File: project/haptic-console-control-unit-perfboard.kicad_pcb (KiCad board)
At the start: 2 copper layers, 90 x 144 mm, 36 parts, among them J1 JST-XH-5, J2 JST-XH-5

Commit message: Eliminate collinear wire overlaps in perfboard jumper wiring
The back-side jumper wires are decorative footprints (no pads, no nets,
invisible to DRC), so their only quality bar is legibility -- and 55 pairs
were merging into each other. The prior session's z-tier stagger fixed
mid-span crossings but not collinear overlaps: two wires sharing a row or
column with overlapping spans, which no height offset can hide.

Rewrote the generator around a span registry -- (net, lo, hi, tier) per grid
line, checked at emit time, rejecting any leg that would overlap another net
at the same tier. That makes "no overlaps" true by construction rather than
by inspection. Tiers now come from greedy-colouring the net-conflict graph
instead of bumping individual segments, which could silently recreate an
overlap at the tier it moved to. 268 segments, 0 same-tier overlaps (was 163
segments, 55 overlaps).

Four real bugs surfaced while getting there:

- taps.json was corrupt ground truth: derived from the old wire geometry, it
  recorded elbow corner points as taps, several of which sit on unrelated
  components' pads -- routing to those invents connections that don't exist.
  Rebuilt from wire labels' REF.PIN->REF.PIN text against real pad positions.

- Routing only on pad-free lanes cannot work here: 4 of ~36 columns and 14 of
  ~54 rows are pad-free and all hug the edges, leaving 19 of 37 signal nets
  unroutable. Legs may follow pad lines as long as they don't pass through a pad.

- Not every pad is on the 2.54mm grid (JST rows at y=15.44 vs 15.24). Grid-only
  routing forced a sub-millimetre hop off each such pad, which the stub filter
  then deleted, silently disconnecting nets from their own pins.

- Wires centred on the edge column overhung the board by their tube radius
  despite being in bounds by centreline.

Added verify_v3.py as a standing check: every tap must lie on a wire and each
net's segments must form one connected component. It caught the open-circuit
bug above, whic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
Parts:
- added W1: GND CB3.2->CB4.2, , B.Cu at (17.8, 49.5)
- added W10: GND CB3.2->CB4.2, , B.Cu at (43.2, 111.9)
- added W100: D27 B8.2->J_TEENSY_B.19, , B.Cu at (48.3, 49.5)
- added W101: D27 B8.2->J_TEENSY_B.19, , B.Cu at (47.0, 58.4)
- added W102: D27 B8.2->J_TEENSY_B.19, , B.Cu at (52.1, 61.2)
- added W103: D27 B8.2->J_TEENSY_B.19, , B.Cu at (58.4, 67.4)
- added W104: D24 B5.2->J_TEENSY_B.16, , B.Cu at (77.5, 38.1)
- added W105: D24 B5.2->J_TEENSY_B.16, , B.Cu at (78.7, 48.4)
- added W106: D24 B5.2->J_TEENSY_B.16, , B.Cu at (66.0, 58.7)
- added W107: D24 B5.2->J_TEENSY_B.16, , B.Cu at (53.3, 66.2)
- added W108: D24 B5.2->J_TEENSY_B.16, , B.Cu at (52.1, 73.7)
- added W109: D25 B6.2->J_TEENSY_B.17, , B.Cu at (66.0, 39.4)
- added W11: GND CB3.2->CB4.2, , B.Cu at (7.62, 34.3)
- added W110: D25 B6.2->J_TEENSY_B.17, , B.Cu at (62.2, 40.6)
- added W111: D25 B6.2->J_TEENSY_B.17, , B.Cu at (58.4, 49.5)
- added W112: D25 B6.2->J_TEENSY_B.17, , B.Cu at (57.1, 58.4)
- added W113: D25 B6.2->J_TEENSY_B.17, , B.Cu at (55.9, 66.0)
- added W114: D25 B6.2->J_TEENSY_B.17, , B.Cu at (54.6, 73.7)
- added W115: D26 B7.2->J_TEENSY_B.18, , B.Cu at (55.9, 36.9)
- added W116: D26 B7.2->J_TEENSY_B.18, , B.Cu at (55.9, 75.0)
- added W117: D26 B7.2->J_TEENSY_B.18, , B.Cu at (62.2, 35.6)
- added W118: D26 B7.2->J_TEENSY_B.18, , B.Cu at (68.6, 38.1)
- added W119: D26 B7.2->J_TEENSY_B.18, , B.Cu at (72.4, 40.6)
- added W12: GND CB3.2->CB4.2, , B.Cu at (45.7, 34.3)
- added W120: D26 B7.2->J_TEENSY_B.18, , B.Cu at (76.2, 58.4)
- added W121: D26 B7.2->J_TEENSY_B.18, , B.Cu at (66.0, 76.2)
- added W122: D14 CB5.1->J_TEENSY_A.13, , B.Cu at (69.8, 119.4)
- added W123: D14 CB5.1->J_TEENSY_A.13, , B.Cu at (71.1, 104.1)
- added W124: D14 CB5.1->J_TEENSY_A.13, , B.Cu at (61.0, 88.9)
- added W125: D14 CB5.1->J_TEENSY_A.13, , B.Cu at (50.8, 55.9)
- added W126: D14 CB5.1->J_TEENSY_A.13, , B.Cu at (50.8, 81.3)
- added W127: D14 CB5.1->J_TEENSY_A.13, , B.Cu at (49.5, 73.7)
- added W128: D14 CB5.1->J_TEENSY_A.13, , B.Cu at (48.3, 66.1)
- added W129: D14 CB5.1->J_TEENSY_A.13, , B.Cu at (49.5, 58.4)
- added W13: GND CB3.2->CB4.2, , B.Cu at (17.8, 73.7)
- added W130: D14 CB5.1->J_TEENSY_A.13, , B.Cu at (47.0, 53.3)
- added W131: D14 CB5.1->J_TEENSY_A.13, , B.Cu at (43.2, 55.9)
- added W132: D13 CB4.1->J_TEENSY_A.14, , B.Cu at (55.9, 118.1)
- added W133: D13 CB4.1->J_TEENSY_A.14, , B.Cu at (47.0, 116.8)
- added W134: D13 CB4.1->J_TEENSY_A.14, , B.Cu at (38.1, 54.6)
- added W135: D13 CB4.1->J_TEENSY_A.14, , B.Cu at (38.1, 95.3)
- added W136: D13 CB4.1->J_TEENSY_A.14, , B.Cu at (36.8, 73.7)
- added W137: D13 CB4.1->J_TEENSY_A.14, , B.Cu at (35.6, 66.1)
- added W138: D13 CB4.1->J_TEENSY_A.14, , B.Cu at (36.8, 58.4)
- added W139: D13 CB4.1->J_TEENSY_A.14, , B.Cu at (41.9, 50.8)
- added W14: GND CB3.2->CB4.2, , B.Cu at (15.2, 66.0)
- added W140: D13 CB4.1->J_TEENSY_A.14, , B.Cu at (45.7, 54.6)
- added W141: D36 R3.2->J_TEENSY_A.21, , B.Cu at (54.6, 124.5)
- added W142: D36 R3.2->J_TEENSY_A.21, , B.Cu at (55.9, 121.9)
- added W143: D36 R3.2->J_TEENSY_A.21, , B.Cu at (61.0, 119.4)
- added W144: D36 R3.2->J_TEENSY_A.21, , B.Cu at (66.0, 96.5)
- added W145: D36 R3.2->J_TEENSY_A.21, , B.Cu at (64.8, 73.7)
- added W146: D36 R3.2->J_TEENSY_A.21, , B.Cu at (63.5, 66.1)
- added W147: D38 R5.2->J_TEENSY_A.19, , B.Cu at (80.0, 124.5)
- added W148: D38 R5.2->J_TEENSY_A.19, , B.Cu at (81.3, 97.8)
- added W149: D38 R5.2->J_TEENSY_A.19, , B.Cu at (71.1, 71.1)
- added W15: GND CB3.2->CB4.2, , B.Cu at (16.5, 58.4)
- added W150: D38 R5.2->J_TEENSY_A.19, , B.Cu at (61.0, 64.8)
- added W151: D38 R5.2->J_TEENSY_A.19, , B.Cu at (59.7, 58.4)
- added W152: D37 R4.2->J_TEENSY_A.20, , B.Cu at (66.0, 55.9)
- added W153: D37 R4.2->J_TEENSY_A.20, , B.Cu at (66.0, 121.9)
- added W154: D37 R4.2->J_TEENSY_A.20, , B.Cu at (67.3, 119.4)
- added W155: D37 R4.2->J_TEENSY_A.20, , B.Cu at (68.6, 66.1)
- added W156: D37 R4.2->J_TEENSY_A.20, , B.Cu at (68.6, 121.9)
- added W157: D37 R4.2->J_TEENSY_A.20, , B.Cu at (72.4, 124.5)
- added W158: D37 R4.2->J_TEENSY_A.20, , B.Cu at (76.2, 106.7)
- added W159: D37 R4.2->J_TEENSY_A.20, , B.Cu at (73.7, 88.9)
- added W16: GND CB3.2->CB4.2, , B.Cu at (48.3, 49.5)
- added W160: D37 R4.2->J_TEENSY_A.20, , B.Cu at (71.1, 81.3)
- added W161: D37 R4.2->J_TEENSY_A.20, , B.Cu at (69.8, 73.7)
- added W162: D37 R4.2->J_TEENSY_A.20, , B.Cu at (67.3, 58.4)
- added W163: D37 R4.2->J_TEENSY_A.20, , B.Cu at (63.5, 53.3)
- added W164: D37 R4.2->J_TEENSY_A.20, , B.Cu at (61.0, 55.9)
- added W165: D35 NP1.8->J_TEENSY_A.22, , B.Cu at (78.7, 60.0)
- added W166: D35 NP1.8->J_TEENSY_A.22, , B.Cu at (72.4, 61.2)
- added W167: D35 NP1.8->J_TEENSY_A.22, , B.Cu at (66.0, 59.8)
- added W168: D34 NP1.7->J_TEENSY_A.23, , B.Cu at (78.7, 62.4)
- added W169: D34 NP1.7->J_TEENSY_A.23, , B.Cu at (74.9, 63.5)
- added W17: GND CB3.2->CB4.2, , B.Cu at (22.9, 81.4)
- added W170: D34 NP1.7->J_TEENSY_A.23, , B.Cu at (71.1, 61.0)
- added W171: D34 NP1.7->J_TEENSY_A.23, , B.Cu at (69.8, 58.4)
- added W172: D33 NP1.6->J_TEENSY_A.24, , B.Cu at (55.9, 63.7)
- added W173: D33 NP1.6->J_TEENSY_A.24, , B.Cu at (33.0, 61.1)
- added W174: D33 NP1.6->J_TEENSY_A.24, , B.Cu at (31.8, 58.4)
- added W175: D33 NP1.6->J_TEENSY_A.24, , B.Cu at (30.5, 53.3)
- added W176: D33 NP1.6->J_TEENSY_A.24, , B.Cu at (50.8, 48.3)
- added W177: D33 NP1.6->J_TEENSY_A.24, , B.Cu at (71.1, 53.3)
- added W178: D32 NP1.5->J_TEENSY_B.24, , B.Cu at (74.9, 66.2)
- added W179: D32 NP1.5->J_TEENSY_B.24, , B.Cu at (71.1, 69.9)
- added W18: GND CB3.2->CB4.2, , B.Cu at (20.3, 100.5)
- added W180: D31 NP1.4->J_TEENSY_B.23, , B.Cu at (72.4, 68.7)
- added W181: D31 NP1.4->J_TEENSY_B.23, , B.Cu at (66.0, 71.2)
- added W182: D31 NP1.4->J_TEENSY_B.23, , B.Cu at (67.3, 73.7)
- added W183: D30 NP1.3->J_TEENSY_B.22, , B.Cu at (73.7, 71.2)
- added W184: D30 NP1.3->J_TEENSY_B.22, , B.Cu at (68.6, 72.4)
- added W185: D30 NP1.3->J_TEENSY_B.22, , B.Cu at (67.3, 73.7)
- added W186: D0 J1.1->J_TEENSY_B.2, , B.Cu at (19.1, 99.1)
- added W187: D0 J1.1->J_TEENSY_B.2, , B.Cu at (15.2, 86.4)
- added W188: D10 CB1.1->J_TEENSY_B.12, , B.Cu at (24.1, 119.4)
- added W189: D10 CB1.1->J_TEENSY_B.12, , B.Cu at (30.5, 118.1)
- added W19: GND CB3.2->CB4.2, , B.Cu at (21.6, 89.1)
- added W190: D10 CB1.1->J_TEENSY_B.12, , B.Cu at (35.6, 116.9)
- added W191: D10 CB1.1->J_TEENSY_B.12, , B.Cu at (40.6, 95.3)
- added W192: D1 J1.2->J_TEENSY_B.3, , B.Cu at (21.6, 96.6)
- added W193: D1 J1.2->J_TEENSY_B.3, , B.Cu at (20.3, 85.1)
- added W194: D1 J1.2->J_TEENSY_B.3, , B.Cu at (19.1, 73.7)
- added W195: D2 J1.3->J_TEENSY_B.4, , B.Cu at (24.1, 94.1)
- added W196: D2 J1.3->J_TEENSY_B.4, , B.Cu at (25.4, 91.6)
- added W197: D2 J1.3->J_TEENSY_B.4, , B.Cu at (24.1, 89.1)
- added W198: D2 J1.3->J_TEENSY_B.4, , B.Cu at (22.9, 81.4)
- added W199: D2 J1.3->J_TEENSY_B.4, , B.Cu at (21.6, 73.7)
- added W2: GND CB3.2->CB4.2, , B.Cu at (17.8, 114.4)
- added W20: GND CB3.2->CB4.2, , B.Cu at (59.7, 89.1)
- added W200: D3 J1.4->J_TEENSY_B.5, , B.Cu at (25.4, 91.6)
- added W201: D3 J1.4->J_TEENSY_B.5, , B.Cu at (27.9, 90.3)
- added W202: D3 J1.4->J_TEENSY_B.5, , B.Cu at (26.7, 89.1)
- added W203: D3 J1.4->J_TEENSY_B.5, , B.Cu at (25.4, 81.4)
- added W204: D3 J1.4->J_TEENSY_B.5, , B.Cu at (24.1, 73.7)
- added W205: D4 J2.1->J_TEENSY_B.6, , B.Cu at (59.7, 99.1)
- added W206: D4 J2.1->J_TEENSY_B.6, , B.Cu at (58.4, 94.1)
- added W207: D4 J2.1->J_TEENSY_B.6, , B.Cu at (43.2, 89.1)
- added W208: D4 J2.1->J_TEENSY_B.6, , B.Cu at (27.9, 81.4)
- added W209: D4 J2.1->J_TEENSY_B.6, , B.Cu at (26.7, 73.7)
- added W21: GND CB3.2->CB4.2, , B.Cu at (58.4, 100.5)
- added W210: D5 J2.2->J_TEENSY_B.7, , B.Cu at (45.7, 96.6)
- added W211: D5 J2.2->J_TEENSY_B.7, , B.Cu at (30.5, 85.1)
- added W212: D5 J2.2->J_TEENSY_B.7, , B.Cu at (29.2, 73.7)
- added W213: D8 R1.2->J_TEENSY_B.10, , B.Cu at (27.9, 110.5)
- added W214: D8 R1.2->J_TEENSY_B.10, , B.Cu at (31.8, 96.5)
- added W215: D8 R1.2->J_TEENSY_B.10, , B.Cu at (35.6, 85.1)
- added W216: D6 J2.3->J_TEENSY_B.8, , B.Cu at (53.3, 94.1)
- added W217: D6 J2.3->J_TEENSY_B.8, , B.Cu at (45.7, 83.9)
- added W218: D6 J2.3->J_TEENSY_B.8, , B.Cu at (44.5, 73.7)
- added W219: D6 J2.3->J_TEENSY_B.8, , B.Cu at (43.2, 72.4)
- added W22: +3V3 S6.2->R12.2, , B.Cu at (44.5, 25.4)
- added W220: D6 J2.3->J_TEENSY_B.8, , B.Cu at (36.8, 71.2)
- added W221: D6 J2.3->J_TEENSY_B.8, , B.Cu at (30.5, 72.4)
- added W222: D11 CB2.1->J_TEENSY_B.13, , B.Cu at (36.8, 119.4)
- added W223: D11 CB2.1->J_TEENSY_B.13, , B.Cu at (43.2, 92.8)
- added W224: D11 CB2.1->J_TEENSY_B.13, , B.Cu at (43.2, 118.1)
- added W225: D11 CB2.1->J_TEENSY_B.13, , B.Cu at (44.5, 116.9)
- added W226: D11 CB2.1->J_TEENSY_B.13, , B.Cu at (45.7, 114.4)
- added W227: D11 CB2.1->J_TEENSY_B.13, , B.Cu at (44.5, 111.9)
- added W228: D7 J2.4->J_TEENSY_B.9, , B.Cu at (54.6, 91.6)
- added W229: D7 J2.4->J_TEENSY_B.9, , B.Cu at (48.3, 82.6)
- added W23: +3V3 S6.2->R12.2, , B.Cu at (50.8, 29.2)
- added W230: D7 J2.4->J_TEENSY_B.9, , B.Cu at (47.0, 73.7)
- added W231: D7 J2.4->J_TEENSY_B.9, , B.Cu at (45.7, 72.4)
- added W232: D7 J2.4->J_TEENSY_B.9, , B.Cu at (39.4, 71.1)
- added W233: D7 J2.4->J_TEENSY_B.9, , B.Cu at (33.0, 72.4)
- added W234: D9 R2.2->J_TEENSY_B.11, , B.Cu at (36.8, 124.5)
- added W235: D9 R2.2->J_TEENSY_B.11, , B.Cu at (33.0, 120.7)
- added W236: D9 R2.2->J_TEENSY_B.11, , B.Cu at (21.6, 116.8)
- added W237: D9 R2.2->J_TEENSY_B.11, , B.Cu at (10.2, 92.8)
- added W238: D9 R2.2->J_TEENSY_B.11, , B.Cu at (24.1, 68.7)
- added W239: D9 R2.2->J_TEENSY_B.11, , B.Cu at (38.1, 71.2)
- added W24: +3V3 S6.2->R12.2, , B.Cu at (63.5, 29.2)
- added W240: D12 CB3.1->J_TEENSY_B.14, , B.Cu at (43.2, 118.1)
- added W241: D12 CB3.1->J_TEENSY_B.14, , B.Cu at (44.5, 116.9)
- added W242: D12 CB3.1->J_TEENSY_B.14, , B.Cu at (45.7, 95.3)
- added W243: D28 NP1.1->J_TEENSY_B.20, , B.Cu at (78.7, 82.6)
- added W244: D28 NP1.1->J_TEENSY_B.20, , B.Cu at (69.8, 89.1)
- added W245: D28 NP1.1->J_TEENSY_B.20, , B.Cu at (61.0, 81.4)
- added W246: D29 NP1.2->J_TEENSY_B.21, , B.Cu at (78.7, 72.5)
- added W247: D29 NP1.2->J_TEENSY_B.21, , B.Cu at (69.8, 71.2)
- added W248: D29 NP1.2->J_TEENSY_B.21, , B.Cu at (61.0, 72.4)
- added W249: D29 NP1.2->J_TEENSY_B.21, , B.Cu at (62.2, 73.7)
- added W25: +3V3 S6.2->R12.2, , B.Cu at (20.3, 58.4)
- added W250: LED_ARM CB1.3->R1.1, , B.Cu at (17.8, 115.6)
- added W251: LED_ARM CB1.3->R1.1, , B.Cu at (16.5, 116.9)
- added W252: LED_ARM CB1.3->R1.1, , B.Cu at (15.2, 120.7)
- added W253: LED_ARM CB1.3->R1.1, , B.Cu at (16.5, 124.5)
- added W254: LED_EN CB2.3->R2.1, , B.Cu at (30.5, 115.6)
- added W255: LED_EN CB2.3->R2.1, , B.Cu at (30.5, 121.9)
- added W256: LED_EN CB2.3->R2.1, , B.Cu at (29.2, 116.8)
- added W257: LED_EN CB2.3->R2.1, , B.Cu at (27.9, 118.1)
- added W258: LED_EN CB2.3->R2.1, , B.Cu at (29.2, 119.4)
- added W259: LED_SFT CB3.3->R3.1, , B.Cu at (43.2, 115.6)
- added W26: +3V3 S6.2->R12.2, , B.Cu at (22.9, 41.9)
- added W260: LED_SFT CB3.3->R3.1, , B.Cu at (41.9, 116.9)
- added W261: LED_SFT CB3.3->R3.1, , B.Cu at (40.6, 120.7)
- added W262: LED_SFT CB3.3->R3.1, , B.Cu at (41.9, 124.5)
- added W263: LED_CONF CB4.3->R4.1, , B.Cu at (57.1, 114.4)
- added W264: LED_CONF CB4.3->R4.1, , B.Cu at (58.4, 119.4)
- added W265: LED_CONF CB4.3->R4.1, , B.Cu at (57.1, 124.5)
- added W266: LED_ALT CB5.3->R5.1, , B.Cu at (67.3, 114.4)
- added W267: LED_ALT CB5.3->R5.1, , B.Cu at (66.0, 119.4)
- added W268: LED_ALT CB5.3->R5.1, , B.Cu at (67.3, 124.5)
- added W27: +3V3 S6.2->R12.2, , B.Cu at (64.8, 73.7)
- added W28: +3V3 S6.2->R12.2, , B.Cu at (81.3, 53.3)
- added W29: +3V3 S6.2->R12.2, , B.Cu at (66.0, 33.0)
- added W3: GND CB3.2->CB4.2, , B.Cu at (30.5, 114.4)
- added W30: +5V S6.3->J_TEENSY_A.1, , B.Cu at (44.5, 22.9)
- added W31: +5V S6.3->J_TEENSY_A.1, , B.Cu at (81.3, 22.9)
- added W32: +5V S6.3->J_TEENSY_A.1, , B.Cu at (12.7, 40.7)
- added W33: SCL R13.1->J_TEENSY_A.8, , B.Cu at (44.5, 17.9)
- added W34: SCL R13.1->J_TEENSY_A.8, , B.Cu at (81.3, 17.9)
- added W35: SCL R13.1->J_TEENSY_A.8, , B.Cu at (53.3, 25.5)
- added W36: SCL R13.1->J_TEENSY_A.8, , B.Cu at (33.0, 58.4)
- added W37: SCL R13.1->J_TEENSY_A.8, , B.Cu at (35.6, 38.2)
- added W38: SDA S6.4->R12.1, , B.Cu at (44.5, 20.4)
- added W39: SDA S6.4->R12.1, , B.Cu at (81.3, 20.4)
- added W4: GND CB3.2->CB4.2, , B.Cu at (43.2, 114.4)
- added W40: SDA S6.4->R12.1, , B.Cu at (38.1, 33.0)
- added W41: SDA S6.4->R12.1, , B.Cu at (43.2, 26.7)
- added W42: SDA S6.4->R12.1, , B.Cu at (33.0, 45.7)
- added W43: IRQ1 S1.6->J_TEENSY_A.12, , B.Cu at (6.35, 15.4)
- added W44: IRQ1 S1.6->J_TEENSY_A.12, , B.Cu at (5.08, 37.1)
- added W45: IRQ1 S1.6->J_TEENSY_A.12, , B.Cu at (22.9, 58.7)
- added W46: IRQ1 S1.6->J_TEENSY_A.12, , B.Cu at (40.6, 58.6)
- added W47: IRQ2 S2.6->J_TEENSY_A.11, , B.Cu at (20.3, 15.3)
- added W48: IRQ2 S2.6->J_TEENSY_A.11, , B.Cu at (11.4, 15.2)
- added W49: IRQ2 S2.6->J_TEENSY_A.11, , B.Cu at (2.54, 38.1)
- added W5: GND CB3.2->CB4.2, , B.Cu at (55.9, 114.4)
- added W50: IRQ2 S2.6->J_TEENSY_A.11, , B.Cu at (20.3, 61.0)
- added W51: IRQ2 S2.6->J_TEENSY_A.11, , B.Cu at (38.1, 59.7)
- added W52: IRQ3 S3.6->J_TEENSY_A.10, , B.Cu at (33.0, 16.7)
- added W53: IRQ3 S3.6->J_TEENSY_A.10, , B.Cu at (33.0, 49.5)
- added W54: IRQ3 S3.6->J_TEENSY_A.10, , B.Cu at (31.8, 17.9)
- added W55: IRQ3 S3.6->J_TEENSY_A.10, , B.Cu at (30.5, 29.3)
- added W56: IRQ3 S3.6->J_TEENSY_A.10, , B.Cu at (31.8, 40.6)
- added W57: IRQ3 S3.6->J_TEENSY_A.10, , B.Cu at (34.3, 58.4)
- added W58: IRQ4 S4.6->J_TEENSY_A.18, , B.Cu at (45.7, 16.7)
- added W59: IRQ4 S4.6->J_TEENSY_A.18, , B.Cu at (48.3, 17.9)
- added W6: GND CB3.2->CB4.2, , B.Cu at (68.6, 114.4)
- added W60: IRQ4 S4.6->J_TEENSY_A.18, , B.Cu at (50.8, 21.7)
- added W61: IRQ4 S4.6->J_TEENSY_A.18, , B.Cu at (49.5, 25.4)
- added W62: IRQ4 S4.6->J_TEENSY_A.18, , B.Cu at (48.3, 33.0)
- added W63: IRQ4 S4.6->J_TEENSY_A.18, , B.Cu at (52.1, 40.6)
- added W64: IRQ4 S4.6->J_TEENSY_A.18, , B.Cu at (55.9, 49.5)
- added W65: IRQ6 S6.6->J_TEENSY_A.16, , B.Cu at (71.1, 16.7)
- added W66: IRQ6 S6.6->J_TEENSY_A.16, , B.Cu at (73.7, 17.9)
- added W67: IRQ6 S6.6->J_TEENSY_A.16, , B.Cu at (76.2, 22.9)
- added W68: IRQ6 S6.6->J_TEENSY_A.16, , B.Cu at (78.7, 27.9)
- added W69: IRQ6 S6.6->J_TEENSY_A.16, , B.Cu at (81.3, 44.5)
- added W7: GND CB3.2->CB4.2, , B.Cu at (41.9, 40.6)
- added W70: IRQ6 S6.6->J_TEENSY_A.16, , B.Cu at (66.0, 61.0)
- added W71: IRQ6 S6.6->J_TEENSY_A.16, , B.Cu at (50.8, 59.7)
- added W72: IRQ5 S5.6->J_TEENSY_A.17, , B.Cu at (58.4, 16.7)
- added W73: IRQ5 S5.6->J_TEENSY_A.17, , B.Cu at (57.1, 17.9)
- added W74: IRQ5 S5.6->J_TEENSY_A.17, , B.Cu at (55.9, 25.5)
- added W75: IRQ5 S5.6->J_TEENSY_A.17, , B.Cu at (54.6, 33.0)
- added W76: IRQ5 S5.6->J_TEENSY_A.17, , B.Cu at (53.3, 45.7)
- added W77: D20 B1.2->J_TEENSY_A.7, , B.Cu at (10.2, 38.1)
- added W78: D20 B1.2->J_TEENSY_A.7, , B.Cu at (12.7, 36.9)
- added W79: D20 B1.2->J_TEENSY_A.7, , B.Cu at (17.8, 35.6)
- added W8: GND CB3.2->CB4.2, , B.Cu at (14.0, 27.9)
- added W80: D20 B1.2->J_TEENSY_A.7, , B.Cu at (22.9, 38.1)
- added W81: D20 B1.2->J_TEENSY_A.7, , B.Cu at (25.4, 40.6)
- added W82: D20 B1.2->J_TEENSY_A.7, , B.Cu at (27.9, 49.5)
- added W83: D21 B2.2->J_TEENSY_A.6, , B.Cu at (17.8, 39.4)
- added W84: D21 B2.2->J_TEENSY_A.6, , B.Cu at (20.3, 40.6)
- added W85: D21 B2.2->J_TEENSY_A.6, , B.Cu at (22.9, 49.5)
- added W86: D21 B2.2->J_TEENSY_A.6, , B.Cu at (24.1, 58.4)
- added W87: D23 B4.2->J_TEENSY_A.4, , B.Cu at (38.1, 39.4)
- added W88: D23 B4.2->J_TEENSY_A.4, , B.Cu at (39.4, 40.6)
- added W89: D23 B4.2->J_TEENSY_A.4, , B.Cu at (40.6, 49.5)
- added W9: GND CB3.2->CB4.2, , B.Cu at (57.1, 27.9)
- added W90: D23 B4.2->J_TEENSY_A.4, , B.Cu at (41.9, 58.4)
- added W91: D23 B4.2->J_TEENSY_A.4, , B.Cu at (43.2, 59.8)
- added W92: D23 B4.2->J_TEENSY_A.4, , B.Cu at (31.8, 61.2)
- added W93: D23 B4.2->J_TEENSY_A.4, , B.Cu at (20.3, 59.8)
- added W94: D22 B3.2->J_TEENSY_A.5, , B.Cu at (24.1, 38.1)
- added W95: D22 B3.2->J_TEENSY_A.5, , B.Cu at (20.3, 48.3)
- added W96: D22 B3.2->J_TEENSY_A.5, , B.Cu at (21.6, 58.4)
- added W97: D27 B8.2->J_TEENSY_B.19, , B.Cu at (45.7, 39.4)
- added W98: D27 B8.2->J_TEENSY_B.19, , B.Cu at (45.7, 59.8)
- added W99: D27 B8.2->J_TEENSY_B.19, , B.Cu at (47.0, 40.6)

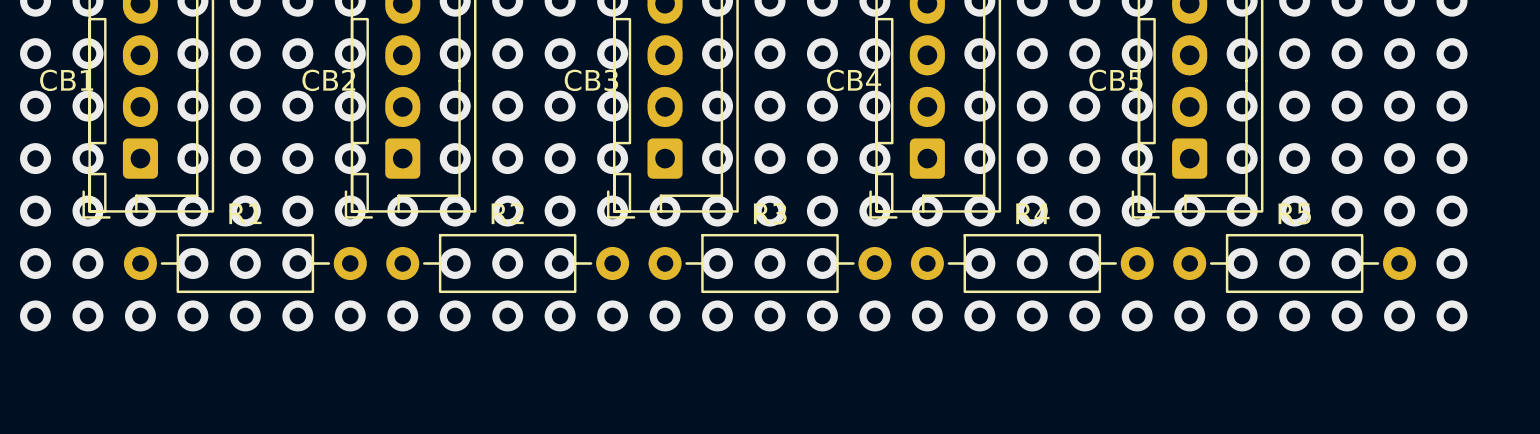
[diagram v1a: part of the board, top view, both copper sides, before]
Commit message: Move LED resistors R1-R5 from hole row 49 to row 48
The board was built with the resistors one row up from where the layout
put them, so move the layout to match the hardware instead of reworking
the board.

R1 Z48/V48, R2 U48/Q48, R3 P48/L48, R4 K48/G48, R5 F48/B48. Only the five
resistors and the ten wires that tap them moved; every other footprint,
wire ref and net is untouched, so nothing already soldered is invalidated.
Background hole-grid vias were removed under the new pad positions and
added back at the vacated ones (via/pad totals net out unchanged).

Verified: verify_v3 clean (268 segments, 50 nets, 0 taps off-wire, 0
disconnected, 0 out-of-bounds), 0 same-tier wire overlaps, 104/104 guide
grid refs match the board, netlist unchanged (LED_* still CBx.3+Rx.1,
R1.2-R5.2 still D8/D9/D36/D37/D38).

DRC goes 409 -> 478, all of it silk/courtyard overlap from R1-R5 now
crowding CB1-CB5; hole, mask and via counts are identical. Same cause as
the clearance note now in the guide: the JST-XH-4 housing edge lands
0.09 mm from the row-48 hole, so each resistor's pin 1 has to be bent
clear before the connector will seat flat.

Renders and the 1:1 placement template regenerated.

Co-Authored-By: Claude Opus 5 (1M context) <noreply@anthropic.com>
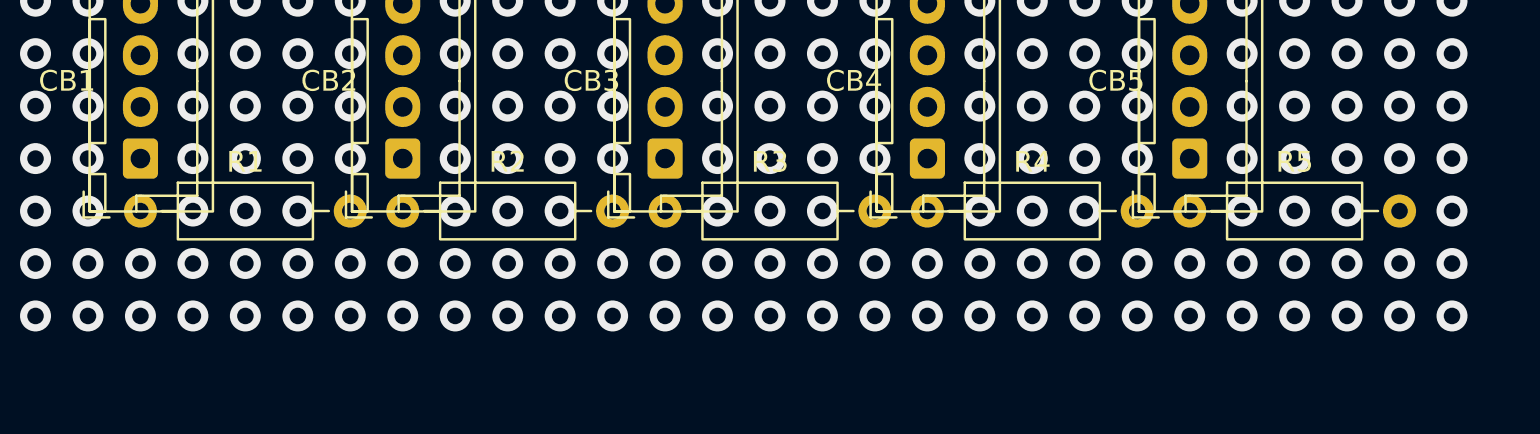
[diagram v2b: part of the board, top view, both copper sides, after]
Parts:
- moved R1 2.54 mm to (17.8, 121.9)
- moved R2 2.54 mm to (30.5, 121.9)
- moved R3 2.54 mm to (43.2, 121.9)
- moved R4 2.54 mm to (55.9, 121.9)
- moved R5 2.54 mm to (68.6, 121.9)
- moved W141 2.54 mm to (54.6, 121.9)
- moved W147 2.54 mm to (80.0, 121.9)
- moved W157 2.54 mm to (72.4, 121.9)
- moved W234 2.54 mm to (36.8, 121.9)
- moved W253 2.54 mm to (16.5, 121.9)
- moved W262 2.54 mm to (41.9, 121.9)
- moved W265 2.54 mm to (57.1, 121.9)
- moved W268 2.54 mm to (67.3, 121.9)
- moved W158 1.27 mm to (76.2, 105.4)
- moved W235 1.27 mm to (33.0, 119.4)
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
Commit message: Remap every GPIO to its nearest Teensy pin, fix stale CB4/D13 doc note
Every connector signal (B1-B8, CB1-5, J1/J2, NP1, LED1-5) now sits on
whichever Teensy pin is physically closest to it on the board instead
of a contiguous functional block, solved as a bipartite matching over
Manhattan wire distance. Schematic labels, the manufactured board's
nets/routing, and the perfboard's hand-wiring layout were all
regenerated from the new scripts/pin_map.json; docs and renders follow.

Also drops the panel wiring guide's leftover "CB4 sits on pin 13"
hazard callout, which the remap made false (D13 moved to NP1's row-0
output) - the equivalent warning already lives in the NP1 section.

Co-Authored-By: Claude Sonnet 5 <noreply@anthropic.com>
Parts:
- removed W204: D3 J1.4->J_TEENSY_B.5, 
- removed W205, W206, W207, W208, W209: D4 J2.1->J_TEENSY_B.6, 
- removed W210, W211, W212: D5 J2.2->J_TEENSY_B.7, 
- removed W213, W214, W215: D8 R1.2->J_TEENSY_B.10, 
- removed W216, W217, W218, W219, W220, W221: D6 J2.3->J_TEENSY_B.8, 
- removed W222, W223, W224, W225, W226, W227: D11 CB2.1->J_TEENSY_B.13, 
- removed W228, W229, W230, W231, W232, W233: D7 J2.4->J_TEENSY_B.9, 
- removed W234, W235, W236, W237, W238, W239: D9 R2.2->J_TEENSY_B.11, 
- removed W240, W241, W242: D12 CB3.1->J_TEENSY_B.14, 
- removed W243, W244, W245: D28 NP1.1->J_TEENSY_B.20, 
- removed W246, W247, W248, W249: D29 NP1.2->J_TEENSY_B.21, 
- removed W250, W251, W252, W253: LED_ARM CB1.3->R1.1, 
- removed W254, W255, W256, W257, W258: LED_EN CB2.3->R2.1, 
- removed W259, W260, W261, W262: LED_SFT CB3.3->R3.1, 
- removed W263, W264, W265: LED_CONF CB4.3->R4.1, 
- removed W266, W267, W268: LED_ALT CB5.3->R5.1, 
- W1, W10, W11, W12, W13, W14, W15, W16, W17, W18, W19, W2, W20, W21, W3, W4, W5, W6, W7, W8, W9: value GND CB3.2->CB4.2 -> GND S1.1->B1.1
- W100, W101, W102, W103: value D27 B8.2->J_TEENSY_B.19 -> D34 B5.2->J_TEENSY_A.23
- W104, W105: value D24 B5.2->J_TEENSY_B.16 -> D13 NP1.5->J_TEENSY_A.14
- W106, W107: value D24 B5.2->J_TEENSY_B.16 -> D41 NP1.8->J_TEENSY_A.16
- W108: value D24 B5.2->J_TEENSY_B.16 -> D40 NP1.7->J_TEENSY_A.17
- W109: value D25 B6.2->J_TEENSY_B.17 -> D40 NP1.7->J_TEENSY_A.17
- W110, W111: value D25 B6.2->J_TEENSY_B.17 -> D37 NP1.6->J_TEENSY_A.20
- W112, W113, W114: value D25 B6.2->J_TEENSY_B.17 -> D36 NP1.4->J_TEENSY_A.21
- W115: value D26 B7.2->J_TEENSY_B.18 -> D36 NP1.4->J_TEENSY_A.21
- W116, W117: value D26 B7.2->J_TEENSY_B.18 -> D30 NP1.3->J_TEENSY_B.22
- W118, W119, W120: value D26 B7.2->J_TEENSY_B.18 -> D1 CB1.1->J_TEENSY_B.3
- W121: value D26 B7.2->J_TEENSY_B.18 -> D2 J1.1->J_TEENSY_B.4
- W122: value D14 CB5.1->J_TEENSY_A.13 -> D2 J1.1->J_TEENSY_B.4
- W123, W124, W125: value D14 CB5.1->J_TEENSY_A.13 -> D3 J1.2->J_TEENSY_B.5
- W126, W127, W128, W129: value D14 CB5.1->J_TEENSY_A.13 -> D4 J1.3->J_TEENSY_B.6
- W130, W131: value D14 CB5.1->J_TEENSY_A.13 -> D5 J1.4->J_TEENSY_B.7
- W132: value D13 CB4.1->J_TEENSY_A.14 -> D5 J1.4->J_TEENSY_B.7
- W133, W134, W135: value D13 CB4.1->J_TEENSY_A.14 -> D7 R1.2->J_TEENSY_B.9
- W136, W137, W138, W139, W140: value D13 CB4.1->J_TEENSY_A.14 -> D6 CB2.1->J_TEENSY_B.8
- W141: value D36 R3.2->J_TEENSY_A.21 -> D6 CB2.1->J_TEENSY_B.8
- W142, W143, W144: value D36 R3.2->J_TEENSY_A.21 -> D8 J2.1->J_TEENSY_B.10
- W145, W146: value D36 R3.2->J_TEENSY_A.21 -> D9 J2.2->J_TEENSY_B.11
- W147: value D38 R5.2->J_TEENSY_A.19 -> D9 J2.2->J_TEENSY_B.11
- W148, W149, W150, W151: value D38 R5.2->J_TEENSY_A.19 -> D10 R2.2->J_TEENSY_B.12
- W152, W153, W154: value D37 R4.2->J_TEENSY_A.20 -> D11 CB3.1->J_TEENSY_B.13
- W155, W156, W157, W158: value D37 R4.2->J_TEENSY_A.20 -> D12 R3.2->J_TEENSY_B.14
- W159, W160: value D37 R4.2->J_TEENSY_A.20 -> D24 J2.3->J_TEENSY_B.16
- W161, W162, W163: value D37 R4.2->J_TEENSY_A.20 -> D25 J2.4->J_TEENSY_B.17
- W164: value D37 R4.2->J_TEENSY_A.20 -> D26 CB4.1->J_TEENSY_B.18
- W165, W166, W167: value D35 NP1.8->J_TEENSY_A.22 -> D26 CB4.1->J_TEENSY_B.18
- W168, W169, W170, W171: value D34 NP1.7->J_TEENSY_A.23 -> D27 NP1.1->J_TEENSY_B.19
- W172, W173, W174, W175: value D33 NP1.6->J_TEENSY_A.24 -> D28 R4.2->J_TEENSY_B.20
- W176, W177: value D33 NP1.6->J_TEENSY_A.24 -> D29 NP1.2->J_TEENSY_B.21
- W178, W179: value D32 NP1.5->J_TEENSY_B.24 -> D29 NP1.2->J_TEENSY_B.21
- W180, W181, W182: value D31 NP1.4->J_TEENSY_B.23 -> D31 CB5.1->J_TEENSY_B.23
- W183, W184, W185: value D30 NP1.3->J_TEENSY_B.22 -> D32 R5.2->J_TEENSY_B.24
- W186, W187: value D0 J1.1->J_TEENSY_B.2 -> LED_ARM CB1.3->R1.1
- W188: value D10 CB1.1->J_TEENSY_B.12 -> LED_ARM CB1.3->R1.1
- W189, W190, W191: value D10 CB1.1->J_TEENSY_B.12 -> LED_EN CB2.3->R2.1
- W192: value D1 J1.2->J_TEENSY_B.3 -> LED_EN CB2.3->R2.1
- W193, W194: value D1 J1.2->J_TEENSY_B.3 -> LED_SFT CB3.3->R3.1
- W195: value D2 J1.3->J_TEENSY_B.4 -> LED_SFT CB3.3->R3.1
- W196, W197, W198: value D2 J1.3->J_TEENSY_B.4 -> LED_CONF CB4.3->R4.1
- W199: value D2 J1.3->J_TEENSY_B.4 -> LED_ALT CB5.3->R5.1
- W200, W201, W202, W203: value D3 J1.4->J_TEENSY_B.5 -> LED_ALT CB5.3->R5.1
- W22, W23, W24, W25, W26, W27, W28, W29: value +3V3 S6.2->R12.2 -> +3V3 S1.2->J_TEENSY_A.3
- W30, W31, W32: value +5V S6.3->J_TEENSY_A.1 -> +5V S1.3->J_TEENSY_A.1
- W33, W34, W35, W36, W37: value SCL R13.1->J_TEENSY_A.8 -> SCL S1.5->S2.5
- W38, W39, W40, W41, W42: value SDA S6.4->R12.1 -> SDA S1.4->S2.4
- W43, W44, W45, W46: value IRQ1 S1.6->J_TEENSY_A.12 -> IRQ1 S1.6->J_TEENSY_A.5
- W47, W48, W49, W50, W51: value IRQ2 S2.6->J_TEENSY_A.11 -> IRQ2 S2.6->J_TEENSY_A.4
- W58, W59, W60: value IRQ4 S4.6->J_TEENSY_A.18 -> IRQ4 S4.6->J_TEENSY_A.13
- W61, W62, W63, W64: value IRQ4 S4.6->J_TEENSY_A.18 -> IRQ5 S5.6->J_TEENSY_A.19
- W65: value IRQ6 S6.6->J_TEENSY_A.16 -> IRQ5 S5.6->J_TEENSY_A.19
- W66, W67, W68, W69, W70, W71: value IRQ6 S6.6->J_TEENSY_A.16 -> IRQ6 S6.6->J_TEENSY_A.24
- W72, W73, W74, W75, W76: value IRQ5 S5.6->J_TEENSY_A.17 -> D0 B1.2->J_TEENSY_B.2
- W77, W78, W79, W80: value D20 B1.2->J_TEENSY_A.7 -> D21 B2.2->J_TEENSY_A.6
- W81, W82: value D20 B1.2->J_TEENSY_A.7 -> D20 B3.2->J_TEENSY_A.7
- W83, W84: value D21 B2.2->J_TEENSY_A.6 -> D20 B3.2->J_TEENSY_A.7
- W85, W86: value D21 B2.2->J_TEENSY_A.6 -> D16 B4.2->J_TEENSY_A.11
- W87, W88: value D23 B4.2->J_TEENSY_A.4 -> D16 B4.2->J_TEENSY_A.11
- W89, W90, W91: value D23 B4.2->J_TEENSY_A.4 -> D15 B8.2->J_TEENSY_A.12
- W92, W93: value D23 B4.2->J_TEENSY_A.4 -> D39 B7.2->J_TEENSY_A.18
- W94, W95: value D22 B3.2->J_TEENSY_A.5 -> D39 B7.2->J_TEENSY_A.18
- W96: value D22 B3.2->J_TEENSY_A.5 -> D35 B6.2->J_TEENSY_A.22
- W97, W98, W99: value D27 B8.2->J_TEENSY_B.19 -> D35 B6.2->J_TEENSY_A.22
- moved W118 96.5 mm to (16.5, 119.4)
- moved W119 79.9 mm to (15.2, 96.5)
- moved W152 67.1 mm to (44.5, 119.4)
- moved W199 66.1 mm to (73.7, 114.4)
- moved W164 63.5 mm to (59.7, 119.4)
- moved W147 63.1 mm to (39.4, 73.7)
- moved W134 62.7 mm to (30.5, 116.8)
- moved W120 61.6 mm to (16.5, 73.7)
- moved W203 60.2 mm to (69.8, 121.9)
- moved W122 59.5 mm to (20.3, 86.4)
- moved W200 59.0 mm to (78.7, 116.9)
- moved W72 55.6 mm to (7.62, 39.4)
- moved W201 55.3 mm to (74.9, 119.4)
- moved W141 55.1 mm to (30.5, 72.4)
- moved W202 54.5 mm to (71.1, 120.7)
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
